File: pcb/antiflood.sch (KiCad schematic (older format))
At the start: 85 parts, among them J1 Barrel_Jack, J10 Screw_Terminal_01x02, J11 Screw_Terminal_01x02, J12 Screw_Terminal_01x02, J13 Screw_Terminal_01x02, J2 01x03, J3 01x03, J4 Conn_02x05_Odd_Even, J5 Conn_02x04_Odd_Even, J6 Conn_02x05_Odd_Even, J7 Conn_02x03_Odd_Even, J8 Screw_Terminal_01x02, J9 Screw_Terminal_01x02, K1 P-5, K2 P-5, Q1 2N3904, Q2 2N3904, SW1 SW_Push, SW2 SW_Push, SW3 SW_Push, U1 LM1117-3.3, U2 ATMEGA328P-AU, U3 LM7805_TO220, U4 MC34063, U5 MC34063, U6 TP4056, Y1 16MHz

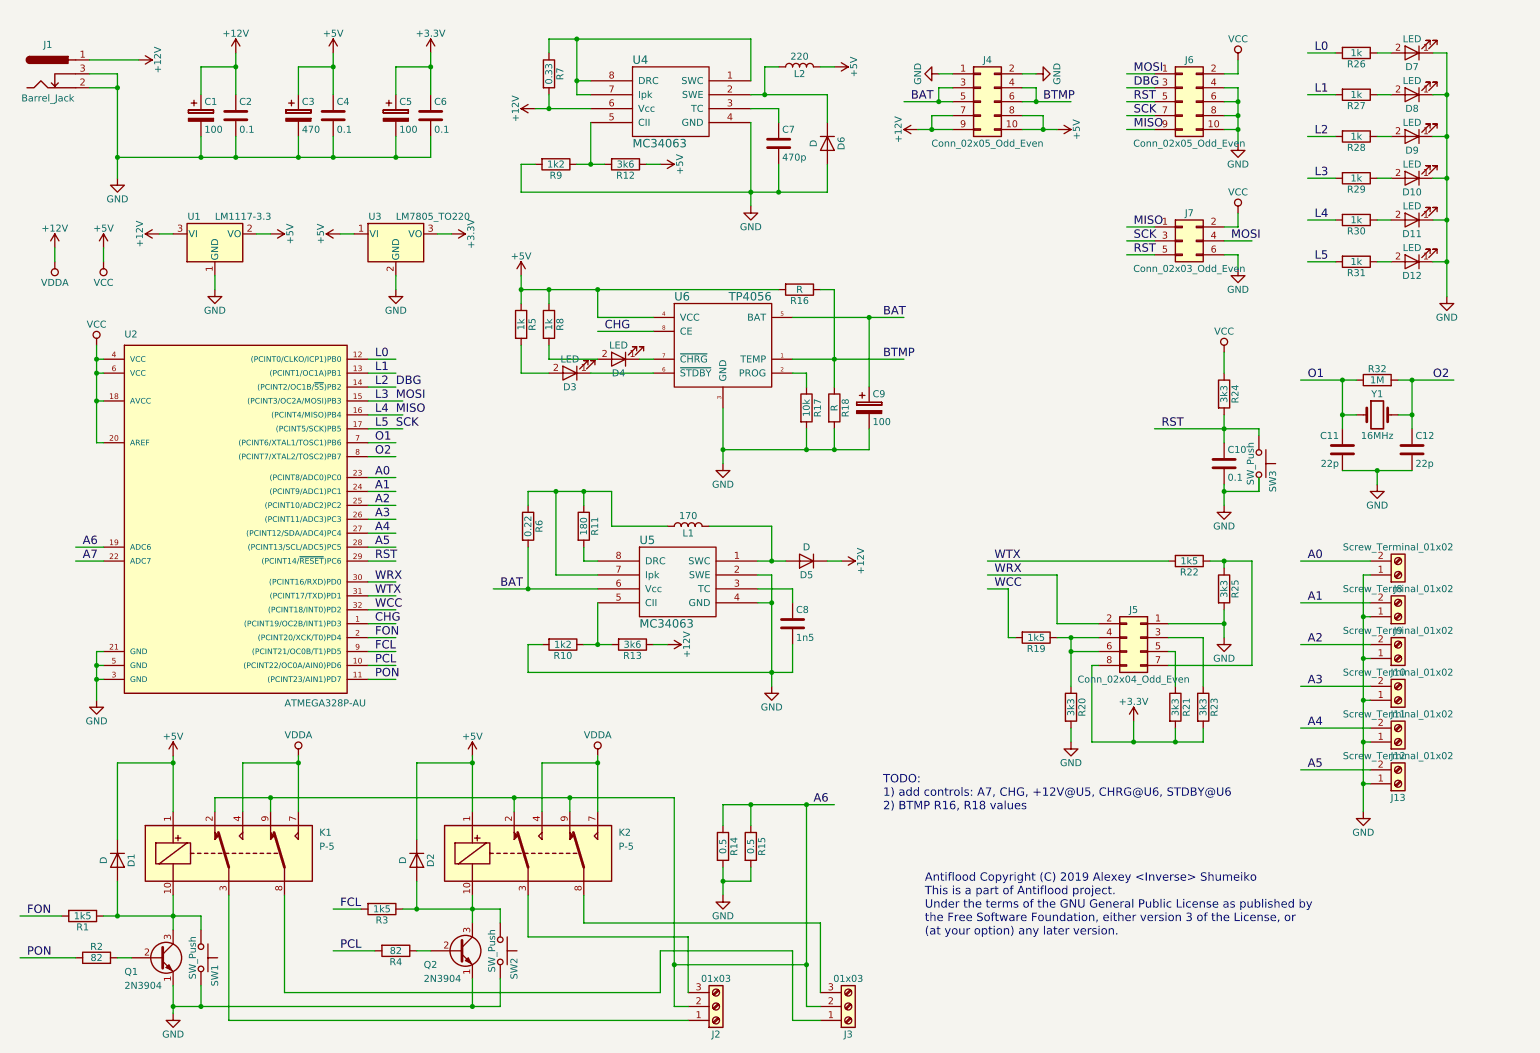
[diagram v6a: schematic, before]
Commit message: Schematics: rework power lines
1. Replace MC34063 with MT3608, which has a plain EN-pin.
2. Automatic controls on booster and charger.
3. CPU awarness about external power presence.
4. CPU awarness of battery voltage.
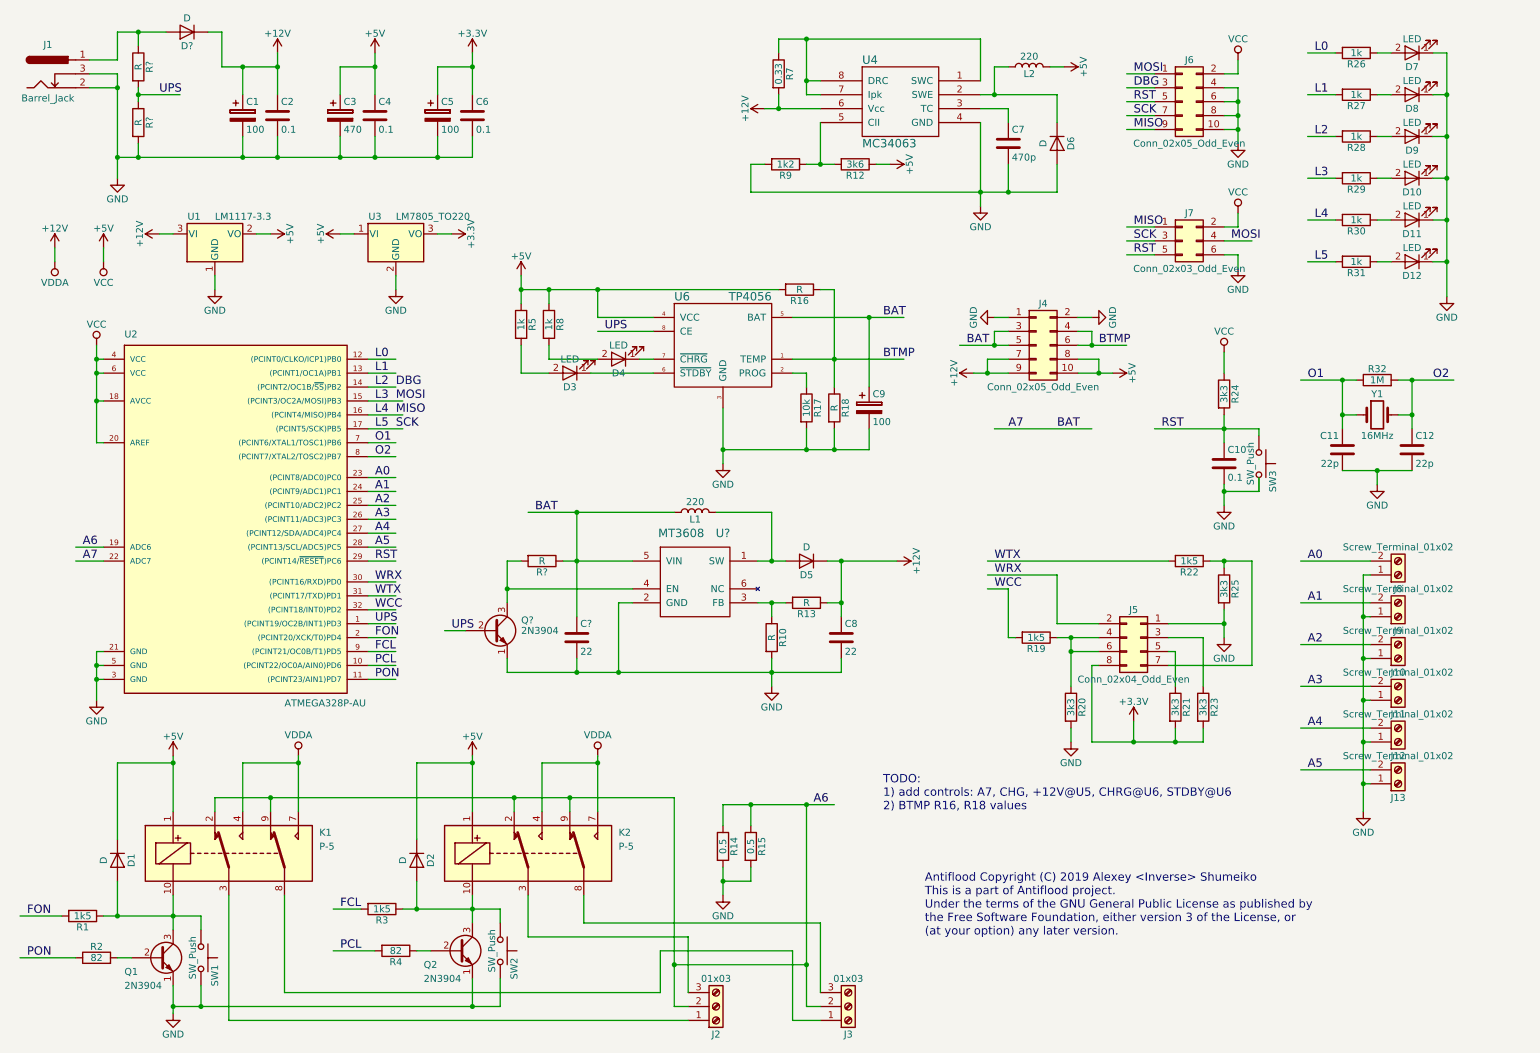
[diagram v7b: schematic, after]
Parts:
- removed R11: 180, Resistors_SMD:R_0805, symbol R
- removed R6: 0.22, Resistors_SMD:R_0805, symbol R
- removed U5: MC34063, SMD_Packages:SOIC-8-N, symbol MC34063
- added C?: 22, symbol C
- added D?: D, symbol D
- added Q?: 2N3904, TO_SOT_Packages_THT:TO-92_Molded_Narrow, symbol 2N3904
- added R? (x3): R, symbol R
- added U?: MT3608, symbol MT3608
- C8: value 1n5 -> 22
- L1: value 170 -> 220
- R10: value 1k2 -> R
- R13: value 3k6 -> R
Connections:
- net labels added: UPS
- net labels removed: CHG
- wire segments 306 -> 310
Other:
- moved on the sheet: C1, C2, C3, C4, C5, C6, C7, C8, D6, J4, L1, L2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

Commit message: Add power supervisor.
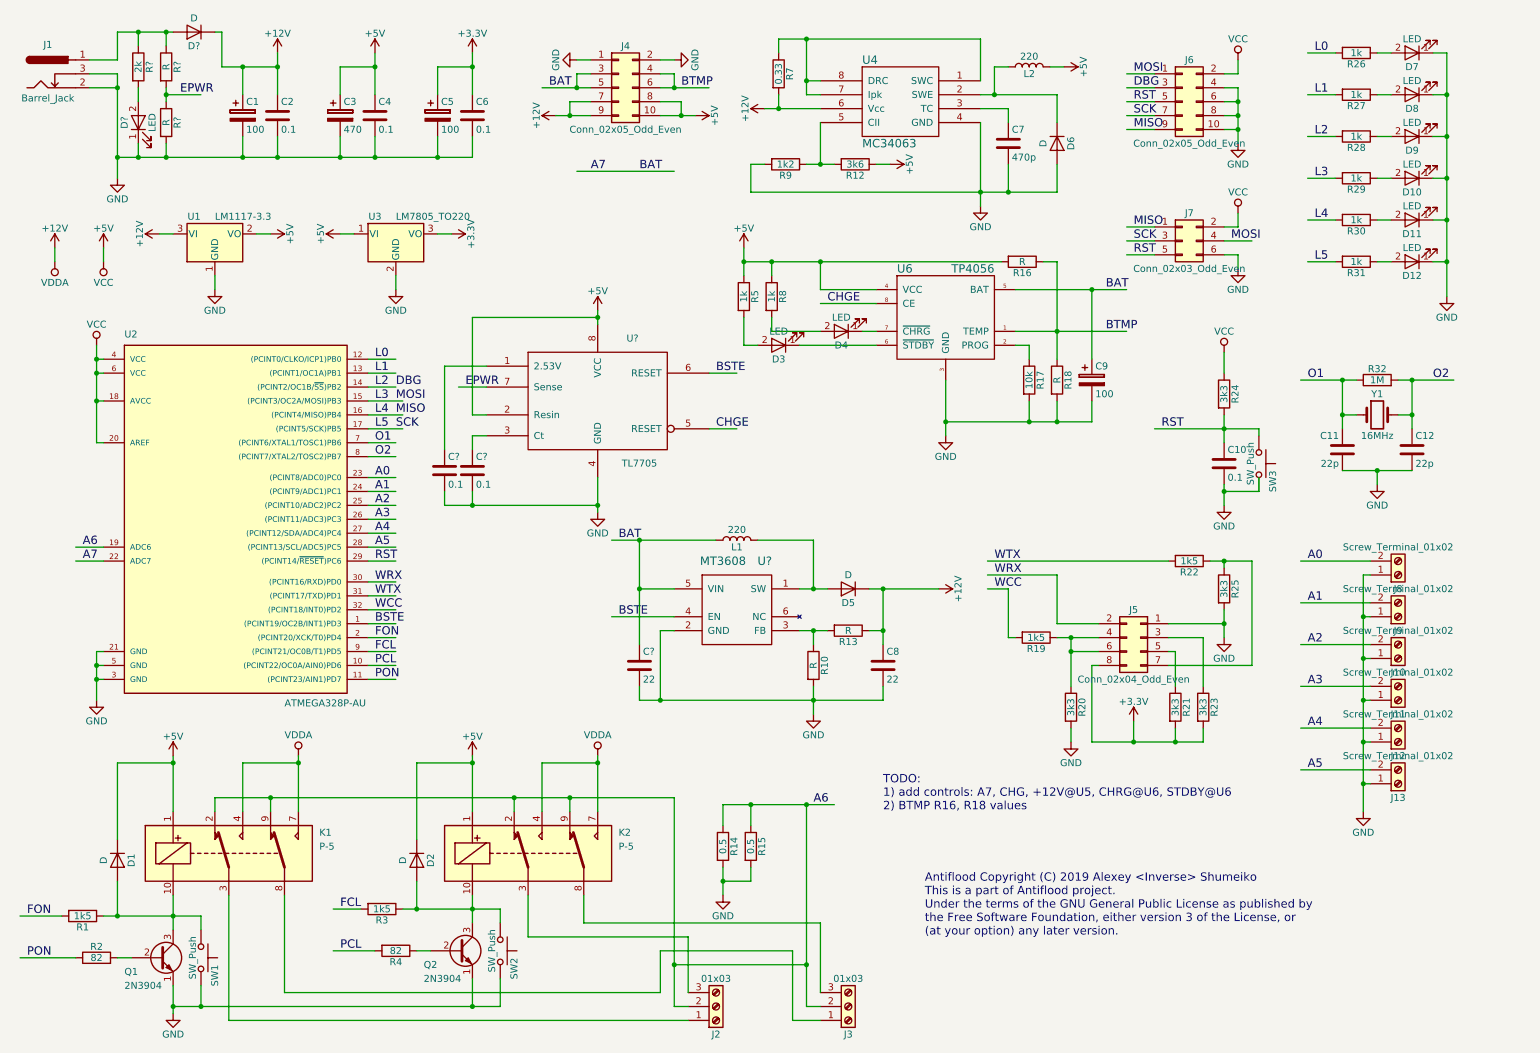
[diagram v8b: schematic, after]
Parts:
- removed Q?: 2N3904, TO_SOT_Packages_THT:TO-92_Molded_Narrow, symbol 2N3904
- removed R?: R, symbol R
- added C? (x2): 0.1, Capacitors_SMD:C_1206, symbol C
- added D?: LED, symbol LED
- added R?: 2k, symbol R
- added U?: TL7705, symbol TL7705
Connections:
- net labels added: BSTE, CHGE, EPWR
- net labels removed: UPS
- wire segments 310 -> 324
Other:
- moved on the sheet: C8, C9, C?, D3, D4, D5, D?, J4, L1, R10, R13, R16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
